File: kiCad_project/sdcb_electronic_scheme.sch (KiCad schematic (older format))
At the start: 94 parts, among them CON1 SD_Card, J1 POWER_12V, J10 B_RIGHT_T, J11 DB9, J2 Arduino_Nano_Header, J4 LEFT_TURN_GYRO, J5 RIGHT_TURN_GYRO, J6 POWER_12V, J7 MOTOR, J8 DB15, J9 B_LEFT_T, U1 74HC595

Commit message: PCB v1
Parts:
- removed U? (x3): OPTO-TRANSISTOR-4, symbol OPTO-TRANSISTOR-4
- added U5, U6, U7: LTV-817, Housings_DIP:DIP-4_W7.62mm_LongPads, symbol LTV-817
- J1, J7: footprint Pin_Headers:Pin_Header_Straight_2x01 -> Connect:AK300-2
- J11: footprint Connect:DB9MD -> Connect:DB9FC
- J12: renamed from J?; value HEADER_2 -> RELAY_CONTROL; footprint (none) -> Pin_Headers:Pin_Header_Straight_1x02
- J13: renamed from J?; footprint (none) -> Connect:AK300-2
- J14: renamed from J?; footprint Pin_Headers:Pin_Header_Straight_2x01 -> Connect:AK300-2
- J6: value POWER_12V -> POWER_MOTOR; footprint Pin_Headers:Pin_Header_Straight_2x01 -> Connect:AK300-2
- J8: footprint (none) -> Connect:DB15FC
- Q1, Q2, Q3: renamed from Q?; footprint SOT-23 -> Housings_TO-92:TO-92_Molded_Wide_Oval
- R11, R12, R13, R14, R15, R16: renamed from R?; footprint (none) -> Resistors_ThroughHole:Resistor_Horizontal_RM10mm
- U2, U3, U4: renamed from U?; footprint (none) -> Housings_DIP:DIP-16_W7.62mm_LongPads
- X1: renamed from X?; footprint (none) -> Buzzer_Beeper_RevA_25Oct2010:MagneticBuzzer_ProSignal_ABT-410-RC_RevA_25Oct2010
- gave numbers to parts that had none: 28
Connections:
- net +12V: now also C2.1
- net GND: now also C2.2
- net at J2.1 (D1/TX): now also U7.1
- net at J2.16 (SCK/D13): now also U6.1
- net at J2.2 (D0/RX): now also U5.1
- net at J8.11 (P111): no longer D17.1 (K)
- net at J8.12 (P12): now also D27.1 (K); no longer D25.1 (K)
- net at J8.14 (P14): now also D25.1 (K); no longer D27.1 (K)
- net at J8.15 (P15): now also D17.1 (K)
- net at Q1.1 (B): now also U5.3
- net at R12.2: now also U5.4
- net at R11.1: now also U5.2
- net at Q3.1 (B): now also U7.3
- net at R16.2: now also U7.4
- net at R14.1: now also U7.2
- net at Q2.1 (B): now also U6.3
- net at R13.1: now also U6.2
- net at R15.2: now also U6.4

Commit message: PCB v2
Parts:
- added C4: 0.1 uF, Capacitors_ThroughHole:C_Disc_D6_P5, symbol C
- U5, U6, U7: footprint Housings_DIP:DIP-4_W7.62mm_LongPads -> Housings_DIP:DIP-4_W7.62mm
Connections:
- net GND: now also C4.2; no longer Current1.1, J6.2, R10.2, RL1.12
- net at J2.5 (D2/INT0), U2.12 (RCLK), U3.12 (RCLK)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: now also C4.1
- net at F2.2, RL1.14, RL3.14: no longer Current1.2, R9.2, RL3.12
- net at J6.1: now also Current1.2, R9.2; no longer F2.1
- new net: Current1.1, R10.2, RL1.12, RL3.12
- new net: F2.1, J6.2
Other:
- note removed: "fuse <11A"
- note removed: "o kaip čia su suagikliu ir srovės ribojimu, nes maitinimas turėtų ateiti iš išorės"
- moved on the sheet: Current1, D11, D34, D36, D9, F2, J6, J7, Q1, Q3, R10, R11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

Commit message: 39 left39 left39 left
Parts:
- added 0R1, 0R2, 0R3, 0R4: 0R, Resistors_ThroughHole:Resistor_Horizontal_RM10mm, symbol R
- added R17: 0R, Resistors_ThroughHole:Resistor_Horizontal_RM15mm, symbol R
- CON1: footprint Connect:SD_Card_Receptacle -> Attend_SD_card_socket:SD_Attend
- Current1: footprint Resistors_ThroughHole:Resistor_Ceramic_Horizontal_L50mm-W14mm-H13mm-p60mm -> Resistor10W_vertical:Resistor_Horizontal_RM15mm
- D32, D33: footprint Diodes_ThroughHole:Diode_DO-41_SOD81_Horizontal_RM10 -> Diode_Smaller:Diode_DO-41_SOD81_Horizontal_RM10_SMALLER
- Q3: footprint Housings_TO-92:TO-92_Molded_Wide_Oval -> Housings_TO-92:TO-92_Inline_Wide
- R1: footprint Resistors_ThroughHole:Resistor_Horizontal_RM10mm -> Resistors_ThroughHole:Resistor_Horizontal_RM15mm
- R8: value 10k -> 1k
- RL2: footprint sun_hold:sun_hold_scb1m1240 -> sun_hold_ras0515:Relay_RAS-0515
- X1: footprint Buzzer_Beeper_RevA_25Oct2010:MagneticBuzzer_ProSignal_ABT-410-RC_RevA_25Oct2010 -> Buzzer_Beeper_RevA_25Oct2010:MagneticBuzzer_ProSignal_ABI-010-RC_RevA_25Oct2010
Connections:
- net at J2.1 (D1/TX): now also U2.11 (SRCLK), U4.11 (SRCLK), 0R4.1; no longer U7.1
- net at J2.11 (D8/ICP): now also U5.1; no longer U2.14 (SER)
- net at J2.16 (SCK/D13): now also C3.2, U1.12 (RCLK); no longer U6.1
- net at J2.2 (D0/RX): now also C4.1, U2.12 (RCLK), U3.12 (RCLK), 0R2.2; no longer U5.1
- net at J10.2, J11.6 (P6), J11.7 (P7)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: now also R17.2; no longer J2.6 (D3/INT1)
- net at U2.9 (~QH): no longer U3.14 (SER)
- net at U3.9 (~QH): now also U2.14 (SER); no longer U4.14 (SER)
- net at R8.1: now also R7.1, R17.1
- net at R8.2: now also D13.1 (K), J2.6 (D3/INT1)
- net at U4.9 (~QH): now also 0R1.2
- new net: J2.10 (D7/AIN1), U7.1
- new net: 0R3.2, J2.5 (D2/INT0)
- new net: J2.7 (D4/T0), U6.1
- new net: 0R4.2, U3.11 (SRCLK)
- new net: 0R1.1, U3.14 (SER)
- new net: 0R2.1, U4.12 (RCLK)
- new net: 0R3.1, U4.14 (SER)

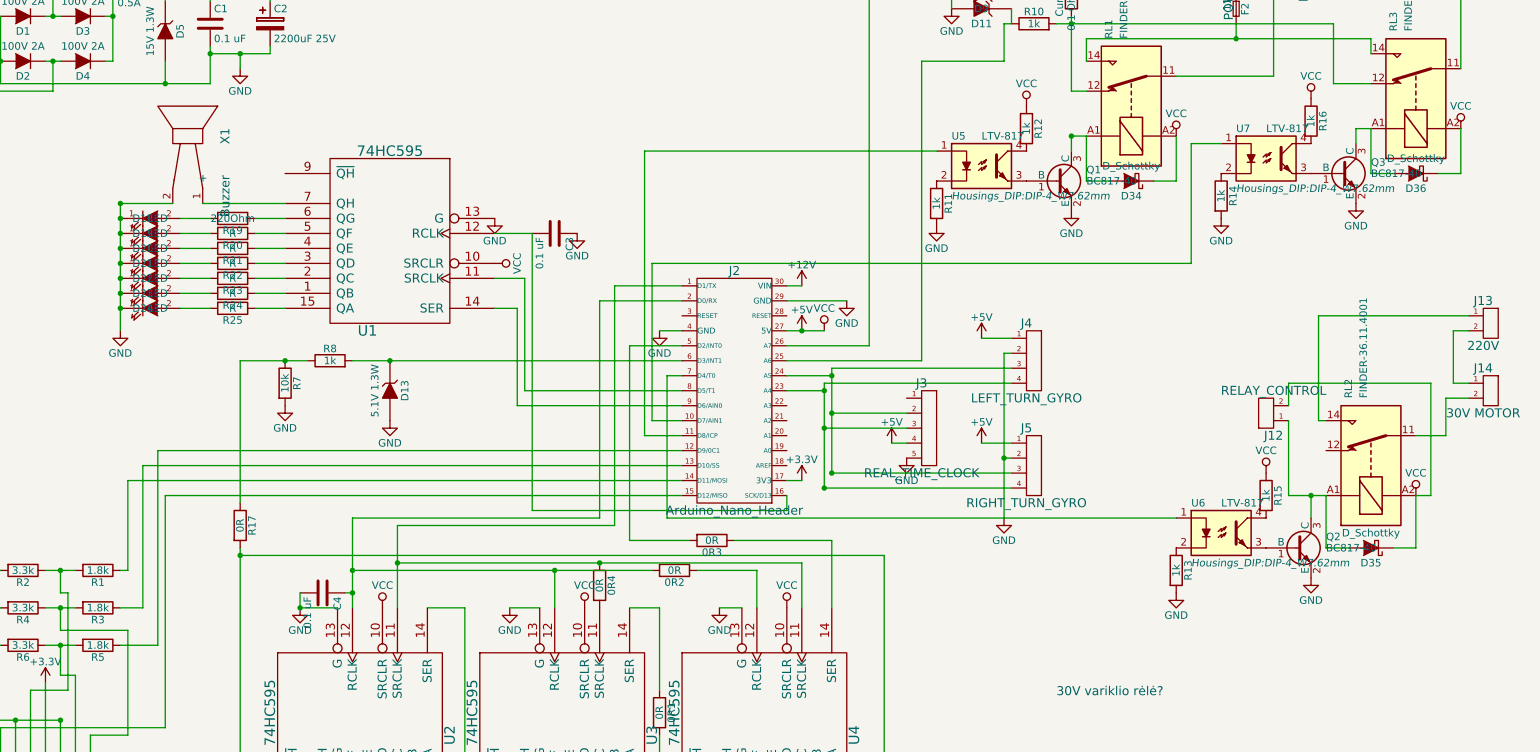
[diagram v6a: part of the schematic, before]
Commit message: LEDs separated
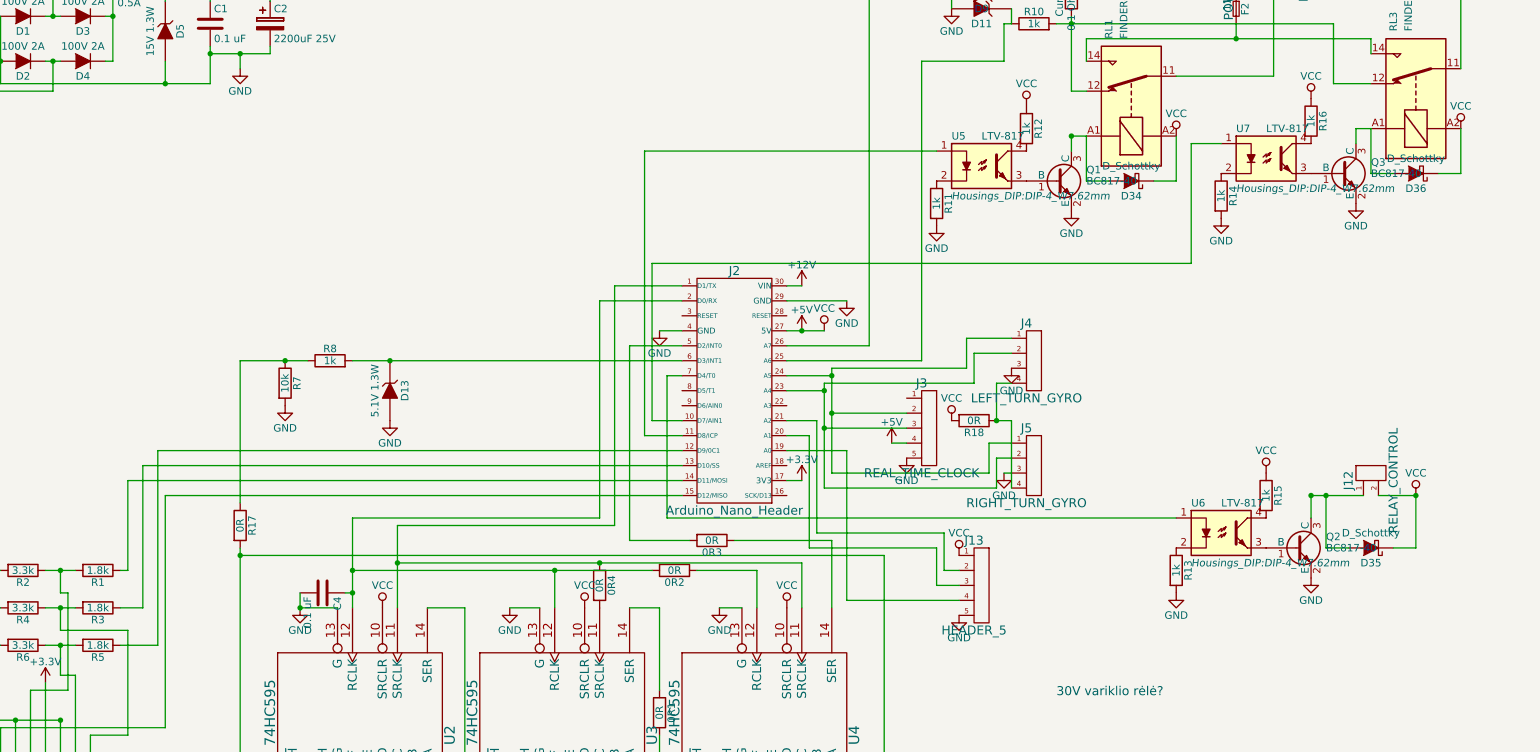
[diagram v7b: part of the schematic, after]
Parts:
- removed C3: 0.1 uF, Capacitors_ThroughHole:C_Disc_D6_P5, symbol C
- removed D18, D19, D20, D21, D22, D23, D24: LED, LEDs:LED-3MM, symbol LED
- removed J13: 220V, Connect:AK300-2, symbol HEADER_2
- removed J14: 30V MOTOR, Connect:AK300-2, symbol HEADER_2
- removed R19: 220Ohm, Resistors_ThroughHole:Resistor_Horizontal_RM10mm, symbol R
- removed R20, R21, R22, R23, R24, R25: R, Resistors_ThroughHole:Resistor_Horizontal_RM10mm, symbol R
- removed RL2: FINDER-36.11.4001, sun_hold_ras0515:Relay_RAS-0515, symbol FINDER-36.11.4001
- removed U1: 74HC595, Housings_DIP:DIP-16_W7.62mm_LongPads, symbol 74HC595
- removed X1: Buzzer, Buzzer_Beeper_RevA_25Oct2010:MagneticBuzzer_ProSignal_ABI-010-RC_RevA_25Oct2010, symbol Buzzer
- added J13: HEADER_5, Pin_Headers:Pin_Header_Straight_1x05, symbol HEADER_5
- added R18: 0R, Resistors_ThroughHole:Resistor_Horizontal_RM15mm, symbol R
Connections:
- net +5V: now also J13.1, R18.2; no longer J4.1, J5.1
- net GND: now also J4.3, J5.3, J13.5; no longer J4.2, J5.2
- net at J2.19 (A0): now also J13.4
- net at J2.20 (A1): now also J13.3
- net at J2.21 (A2): now also J13.2
- net at J2.23 (A4), J3.3: now also J4.2, J5.2; no longer J4.4, J5.4
- net at J2.24 (A5), J3.2: now also J4.1, J5.1; no longer J4.3, J5.3
- new net: J4.4, J5.4, R18.1
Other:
- moved on the sheet: J12

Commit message: Varžtai IN
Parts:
- added C3: 2200uF >6.3V, Capacitors_Elko_ThroughHole:Elko_vert_25x14mm_RM5_CopperClear, symbol CP
- added J14, J15: HEADER_1, Mounting_Holes:MountingHole_3-7mm, symbol HEADER_1
- Q2: footprint Housings_TO-92:TO-92_Molded_Wide_Oval -> Housings_TO-92:TO-92_Inline_Wide
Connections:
- net +5V: now also J4.4, J5.4, R18.1, C3.1
- net GND: now also C3.2, J14.1, J15.1
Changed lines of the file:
@@
 $Comp
 L GND #PWR07
-U 1 1 55BDA311
-P 6550 2850
-F 0 "#PWR07" H 6550 2600 50  0001 C CNN
-F 1 "GND" H 6550 2700 50  0000 C CNN
-F 2 "" H 6550 2850 60  0000 C CNN
-F 3 "" H 6550 2850 60  0000 C CNN
-	1    6550 2850
-	1    0    0    -1
-$EndComp
-$Comp
-L GND #PWR08
 U 1 1 55BDB4FB
 P 5300 3050
-F 0 "#PWR08" H 5300 2800 50  0001 C CNN
+F 0 "#PWR07" H 5300 2800 50  0001 C CNN
 F 1 "GND" H 5300 2900 50  0000 C CNN
 F 2 "" H 5300 3050 60  0000 C CNN
@@
 $EndComp
 $Comp
-L GND #PWR010
+L GND #PWR08
 U 1 1 55BF6554
 P 7600 4000
-F 0 "#PWR010" H 7600 3750 50  0001 C CNN
+F 0 "#PWR08" H 7600 3750 50  0001 C CNN
 F 1 "GND" H 7600 3850 50  0000 C CNN
 F 2 "" H 7600 4000 60  0000 C CNN
@@
 $EndComp
 $Comp
-L GND #PWR011
+L GND #PWR09
 U 1 1 55BB6D26
 P 7250 900
-F 0 "#PWR011" H 7250 650 50  0001 C CNN
+F 0 "#PWR09" H 7250 650 50  0001 C CNN
 F 1 "GND" H 7250 750 50  0000 C CNN
 F 2 "" H 7250 900 60  0000 C CNN
@@
 $EndComp
 $Comp
-L VCC #PWR012
+L VCC #PWR010
 U 1 1 55BBD6FF
 P 6400 3050
-F 0 "#PWR012" H 6400 2900 50  0001 C CNN
+F 0 "#PWR010" H 6400 2900 50  0001 C CNN
 F 1 "VCC" H 6400 3200 50  0000 C CNN
 F 2 "" H 6400 3050 60  0000 C CNN
@@
 wtf? pull-up, pull down ir Kondensatorius\n\n
 $Comp
-L +3.3V #PWR013
+L +3.3V #PWR011
 U 1 1 55C26656
 P 1200 5400
-F 0 "#PWR013" H 1200 5250 50  0001 C CNN
+F 0 "#PWR011" H 1200 5250 50  0001 C CNN
 F 1 "+3.3V" H 1200 5540 50  0000 C CNN
 F 2 "" H 1200 5400 60  0000 C CNN
@@
 $EndComp
 $Comp
-L GND #PWR014
+L GND #PWR012
 U 1 1 55C39A8C
 P 2800 3550
-F 0 "#PWR014" H 2800 3300 50  0001 C CNN
+F 0 "#PWR012" H 2800 3300 50  0001 C CNN
 F 1 "GND" H 2800 3400 50  0000 C CNN
 F 2 "" H 2800 3550 60  0000 C CNN
@@
 $EndComp
 $Comp
-L GND #PWR015
+L GND #PWR013
 U 1 1 55C6252E
 P 6950 3900
-F 0 "#PWR015" H 6950 3650 50  0001 C CNN
+F 0 "#PWR013" H 6950 3650 50  0001 C CNN
 F 1 "GND" H 6950 3750 50  0000 C CNN
 F 2 "" H 6950 3900 60  0000 C CNN
@@
 $EndComp
 $Comp
-L +5V #PWR016
+L +5V #PWR014
 U 1 1 55C6263E
 P 6850 3800
-F 0 "#PWR016" H 6850 3650 50  0001 C CNN
+F 0 "#PWR014" H 6850 3650 50  0001 C CNN
 F 1 "+5V" H 6850 3940 50  0000 C CNN
 F 2 "" H 6850 3800 60  0000 C CNN
@@
 $EndComp
 $Comp
-L GND #PWR017
+L GND #PWR015
 U 1 1 55C22E89
 P 5700 4900
-F 0 "#PWR017" H 5700 4650 50  0001 C CNN
+F 0 "#PWR015" H 5700 4650 50  0001 C CNN
 F 1 "GND" H 5700 4750 50  0000 C CNN
 F 2 "" H 5700 4900 60  0000 C CNN
@@
 $EndComp
 $Comp
-L GND #PWR018
+L GND #PWR016
 U 1 1 55C22F8A
 P 4300 4900
-F 0 "#PWR018" H 4300 4650 50  0001 C CNN
+F 0 "#PWR016" H 4300 4650 50  0001 C CNN
 F 1 "GND" H 4300 4750 50  0000 C CNN
 F 2 "" H 4300 4900 60  0000 C CNN
@@
 $EndComp
 $Comp
-L GND #PWR019
+L GND #PWR017
 U 1 1 55C2308B
 P 2900 4900
-F 0 "#PWR019" H 2900 4650 50  0001 C CNN
+F 0 "#PWR017" H 2900 4650 50  0001 C CNN
 F 1 "GND" H 2900 4750 50  0000 C CNN
 F 2 "" H 2900 4900 60  0000 C CNN
@@
 $EndComp
 $Comp
-L VCC #PWR020
+L VCC #PWR018
 U 1 1 55C27D5D
 P 3450 4900
-F 0 "#PWR020" H 3450 4750 50  0001 C CNN
+F 0 "#PWR018" H 3450 4750 50  0001 C CNN
 F 1 "VCC" H 3450 5050 50  0000 C CNN
 F 2 "" H 3450 4900 60  0000 C CNN
@@
 $EndComp
 $Comp
-L VCC #PWR021
+L VCC #PWR019
 U 1 1 55C283D0
 P 4800 4900
-F 0 "#PWR021" H 4800 4750 50  0001 C CNN
+F 0 "#PWR019" H 4800 4750 50  0001 C CNN
 F 1 "VCC" H 4800 5050 50  0000 C CNN
 F 2 "" H 4800 4900 60  0000 C CNN
@@
 $EndComp
 $Comp
-L VCC #PWR022
+L VCC #PWR020
 U 1 1 55C28761
 P 6150 4900
-F 0 "#PWR022" H 6150 4750 50  0001 C CNN
+F 0 "#PWR020" H 6150 4750 50  0001 C CNN
 F 1 "VCC" H 6150 5050 50  0000 C CNN
 F 2 "" H 6150 4900 60  0000 C CNN
@@
 $EndComp
 $Comp
-L GND #PWR023
+L GND #PWR021
 U 1 1 55C398FF
 P 3500 3650
-F 0 "#PWR023" H 3500 3400 50  0001 C CNN
+F 0 "#PWR021" H 3500 3400 50  0001 C CNN
 F 1 "GND" H 3500 3500 50  0000 C CNN
 F 2 "" H 3500 3650 60  0000 C CNN
@@
 $EndComp
 $Comp
-L GND #PWR024
+L GND #PWR022
 U 1 1 55C334D4
 P 7150 2350
-F 0 "#PWR024" H 7150 2100 50  0001 C CNN
+F 0 "#PWR022" H 7150 2100 50  0001 C CNN
 F 1 "GND" H 7150 2200 50  0000 C CNN
 F 2 "" H 7150 2350 60  0000 C CNN
@@
 $EndComp
 $Comp
-L VCC #PWR025
+L VCC #PWR023
 U 1 1 55C3459B
 P 7750 1550
-F 0 "#PWR025" H 7750 1400 50  0001 C CNN
+F 0 "#PWR023" H 7750 1400 50  0001 C CNN
 F 1 "VCC" H 7750 1700 50  0000 C CNN
 F 2 "" H 7750 1550 60  0000 C CNN
@@
 $EndComp
 $Comp
-L VCC #PWR026
+L VCC #PWR024
 U 1 1 55C34C2F
 P 8750 1750
-F 0 "#PWR026" H 8750 1600 50  0001 C CNN
+F 0 "#PWR024" H 8750 1600 50  0001 C CNN
 F 1 "VCC" H 8750 1900 50  0000 C CNN
 F 2 "" H 8750 1750 60  0000 C CNN
@@
 $EndComp
 $Comp
-L GND #PWR027
+L GND #PWR025
 U 1 1 55C35DCF
 P 8050 2250
-F 0 "#PWR027" H 8050 2000 50  0001 C CNN
+F 0 "#PWR025" H 8050 2000 50  0001 C CNN
 F 1 "GND" H 8050 2100 50  0000 C CNN
 F 2 "" H 8050 2250 60  0000 C CNN
@@
 $EndComp
 $Comp
-L GND #PWR028
+L GND #PWR026
 U 1 1 55C38D13
 P 9950 2200
-F 0 "#PWR028" H 9950 1950 50  0001 C CNN
+F 0 "#PWR026" H 9950 1950 50  0001 C CNN
 F 1 "GND" H 9950 2050 50  0000 C CNN
 F 2 "" H 9950 2200 60  0000 C CNN
@@
 $EndComp
 $Comp
-L VCC #PWR029
+L VCC #PWR027
 U 1 1 55C392E8
 P 9650 1500
-F 0 "#PWR029" H 9650 1350 50  0001 C CNN
+F 0 "#PWR027" H 9650 1350 50  0001 C CNN
 F 1 "VCC" H 9650 1650 50  0000 C CNN
 F 2 "" H 9650 1500 60  0000 C CNN
@@
 $EndComp
 $Comp
-L VCC #PWR030
+L VCC #PWR028
 U 1 1 55C39E36
 P 10650 1700
-F 0 "#PWR030" H 10650 1550 50  0001 C CNN
+F 0 "#PWR028" H 10650 1550 50  0001 C CNN
 F 1 "VCC" H 10650 1850 50  0000 C CNN
 F 2 "" H 10650 1700 60  0000 C CNN
@@
 $EndComp
 $Comp
-L GND #PWR031
+L GND #PWR029
 U 1 1 55C45404
 P 9050 2300
-F 0 "#PWR031" H 9050 2050 50  0001 C CNN
+F 0 "#PWR029" H 9050 2050 50  0001 C CNN
 F 1 "GND" H 9050 2150 50  0000 C CNN
 F 2 "" H 9050 2300 60  0000 C CNN
@@
 F 0 "Q2" H 9750 4575 50  0000 L CNN
 F 1 "BC817-40" H 9750 4500 50  0000 L CNN
-F 2 "Housings_TO-92:TO-92_Molded_Wide_Oval" H 9750 4425 50  0001 L CIN
+F 2 "Housings_TO-92:TO-92_Inline_Wide" H 9750 4425 50  0001 L CIN
 F 3 "" H 9550 4500 50  0000 L CNN
 	1    9550 4500
@@
 $EndComp
 $Comp
-L GND #PWR032
+L GND #PWR030
 U 1 1 55C60FBE
 P 9650 4700
-F 0 "#PWR032" H 9650 4450 50  0001 C CNN
+F 0 "#PWR030" H 9650 4450 50  0001 C CNN
 F 1 "GND" H 9650 4550 50  0000 C CNN
 F 2 "" H 9650 4700 60  0000 C CNN
@@
 $EndComp
 $Comp
-L VCC #PWR033
+L VCC #PWR031
 U 1 1 55C61383
 P 9350 4000
-F 0 "#PWR033" H 9350 3850 50  0001 C CNN
+F 0 "#PWR031" H 9350 3850 50  0001 C CNN
 F 1 "VCC" H 9350 4150 50  0000 C CNN
 F 2 "" H 9350 4000 60  0000 C CNN
@@
 $EndComp
 $Comp
-L GND #PWR034
+L GND #PWR032
 U 1 1 55C61A26
 P 8750 4800
-F 0 "#PWR034" H 8750 4550 50  0001 C CNN
+F 0 "#PWR032" H 8750 4550 50  0001 C CNN
 F 1 "GND" H 8750 4650 50  0000 C CNN
 F 2 "" H 8750 4800 60  0000 C CNN
@@
 $EndComp
 $Comp
-L VCC #PWR035
+L VCC #PWR033
 U 1 1 55C63AFD
 P 10350 4150
-F 0 "#PWR035" H 10350 4000 50  0001 C CNN
+F 0 "#PWR033" H 10350 4000 50  0001 C CNN
 F 1 "VCC" H 10350 4300 50  0000 C CNN
 F 2 "" H 10350 4150 60  0000 C CNN
@@
 	1300 5350 1300 5150
 Wire Wire Line
-	6150 3050 6400 3050
+	6150 3050 6850 3050
 Wire Wire Line
 	6250 4050 6150 4050
@@
 	2500 1300 2500 1200
 Wire Wire Line
-	2300 1200 2700 1200
+	2300 1200 3150 1200
 Connection ~ 2500 1200
 Connection ~ 2000 800
@@
 	7400 3400 7400 3200
 $Comp
-L GND #PWR036
+L GND #PWR034
 U 1 1 55C75B8D
 P 7650 3300
-F 0 "#PWR036" H 7650 3050 50  0001 C CNN
+F 0 "#PWR034" H 7650 3050 50  0001 C CNN
 F 1 "GND" H 7650 3150 50  0000 C CNN
 F 2 "" H 7650 3300 60  0000 C CNN
@@
 	7650 3400 7550 3400
 Wire Wire Line
-	7550 3400 7550 3650
+	7550 3400 7550 3750
 $Comp
 L R R18
@@
 $EndComp
 $Comp
-L GND #PWR037
+L GND #PWR035
 U 1 1 55C85F11
 P 7300 4950
-F 0 "#PWR037" H 7300 4700 50  0001 C CNN
+F 0 "#PWR035" H 7300 4700 50  0001 C CNN
 F 1 "GND" H 7300 4800 50  0000 C CNN
 F 2 "" H 7300 4950 60  0000 C CNN
@@
 $EndComp
 $Comp
-L VCC #PWR038
+L VCC #PWR036
 U 1 1 55C86018
 P 7300 4550
-F 0 "#PWR038" H 7300 4400 50  0001 C CNN
+F 0 "#PWR036" H 7300 4400 50  0001 C CNN
 F 1 "VCC" H 7300 4700 50  0000 C CNN
 F 2 "" H 7300 4550 60  0000 C CNN
@@
 	6550 4850 7300 4850
 $Comp
-L VCC #PWR?
+L VCC #PWR037
 U 1 1 55C8CF04
 P 7250 3650
-F 0 "#PWR?" H 7250 3500 50  0001 C CNN
+F 0 "#PWR037" H 7250 3500 50  0001 C CNN
 F 1 "VCC" H 7250 3800 50  0000 C CNN
 F 2 "" H 7250 3650 60  0000 C CNN
@@
 Wire Wire Line
 	6350 3650 6150 3650
+Wire Wire Line
+	7250 3650 7250 3750
+Wire Wire Line
+	7250 3750 7550 3750
+Connection ~ 7250 3650
+$Comp
+L CP C3
+U 1 1 55C79B70
+P 6850 2900
+F 0 "C3" H 6875 3000 50  0000 L CNN
+F 1 "2200uF >6.3V" H 6875 2800 50  0000 L CNN
+F 2 "Capacitors_Elko_ThroughHole:Elko_vert_25x14mm_RM5_CopperClear" H 6888 2750 30  0001 C CNN
+F 3 "" H 6850 2900 60  0000 C CNN
+	1    6850 2900
+	-1   0    0    1
+$EndComp
+Wire Wire Line
+	6550 2850 6550 2750
+Wire Wire Line
+	6550 2750 7150 2750
+$Comp
+L GND #PWR038
+U 1 1 55C7C6BC
+P 7150 2750
+F 0 "#PWR038" H 7150 2500 50  0001 C CNN
+F 1 "GND" H 7150 2600 50  0000 C CNN
+F 2 "" H 7150 2750 60  0000 C CNN
+F 3 "" H 7150 2750 60  0000 C CNN
+	1    7150 2750
+	1    0    0    -1
+$EndComp
+Connection ~ 6850 2750
+Connection ~ 6400 3050
+$Comp
+L HEADER_1 J14
+U 1 1 55C7DBF9
+P 2900 1500
+F 0 "J14" H 2900 1650 60  0000 C CNN
+F 1 "HEADER_1" H 2900 1350 60  0000 C CNN
+F 2 "Mounting_Holes:MountingHole_3-7mm" H 2900 1500 60  0001 C CNN
+F 3 "" H 2900 1500 60  0000 C CNN
+	1    2900 1500
+	1    0    0    -1
+$EndComp
+Wire Wire Line
+	2800 1200 2800 1500
+Connection ~ 2700 1200
+$Comp
+L HEADER_1 J15
+U 1 1 55C7F2A3
+P 3250 1500
+F 0 "J15" H 3250 1650 60  0000 C CNN
+F 1 "HEADER_1" H 3250 1350 60  0000 C CNN
+F 2 "Mounting_Holes:MountingHole_3-7mm" H 3250 1500 60  0001 C CNN
+F 3 "" H 3250 1500 60  0000 C CNN
+	1    3250 1500
+	1    0    0    -1
+$EndComp
+Wire Wire Line
+	3150 1200 3150 1500
+Connection ~ 2800 1200
 $EndSCHEMATC
